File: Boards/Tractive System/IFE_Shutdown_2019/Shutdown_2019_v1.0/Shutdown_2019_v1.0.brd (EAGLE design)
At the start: 88.9 x 76.2 mm, 193 parts, among them Q1 DMN6140L-7, Q10 DMN6140L-7, Q11 DMP3099L-7, Q12 IRLML6346PBF, Q13 IRLML6346PBF, Q14 IRLML6346PBF, Q15 DMP3099L-7, Q16 DMN6140L-7, Q17 IRLML6346PBF, Q18 DMN6140L-7, Q2 DMN6140L-7, Q20 DMN6140L-7, Q21 DMN6140L-7, Q3 DMN6140L-7, Q4 DMN6140L-7, Q5 DMN6140L-7, Q6 DMP3099L-7, Q7 DMN6140L-7, Q9 DMN6140L-7, U1 STM32F103CBT6, U2 STM32F103CBT6

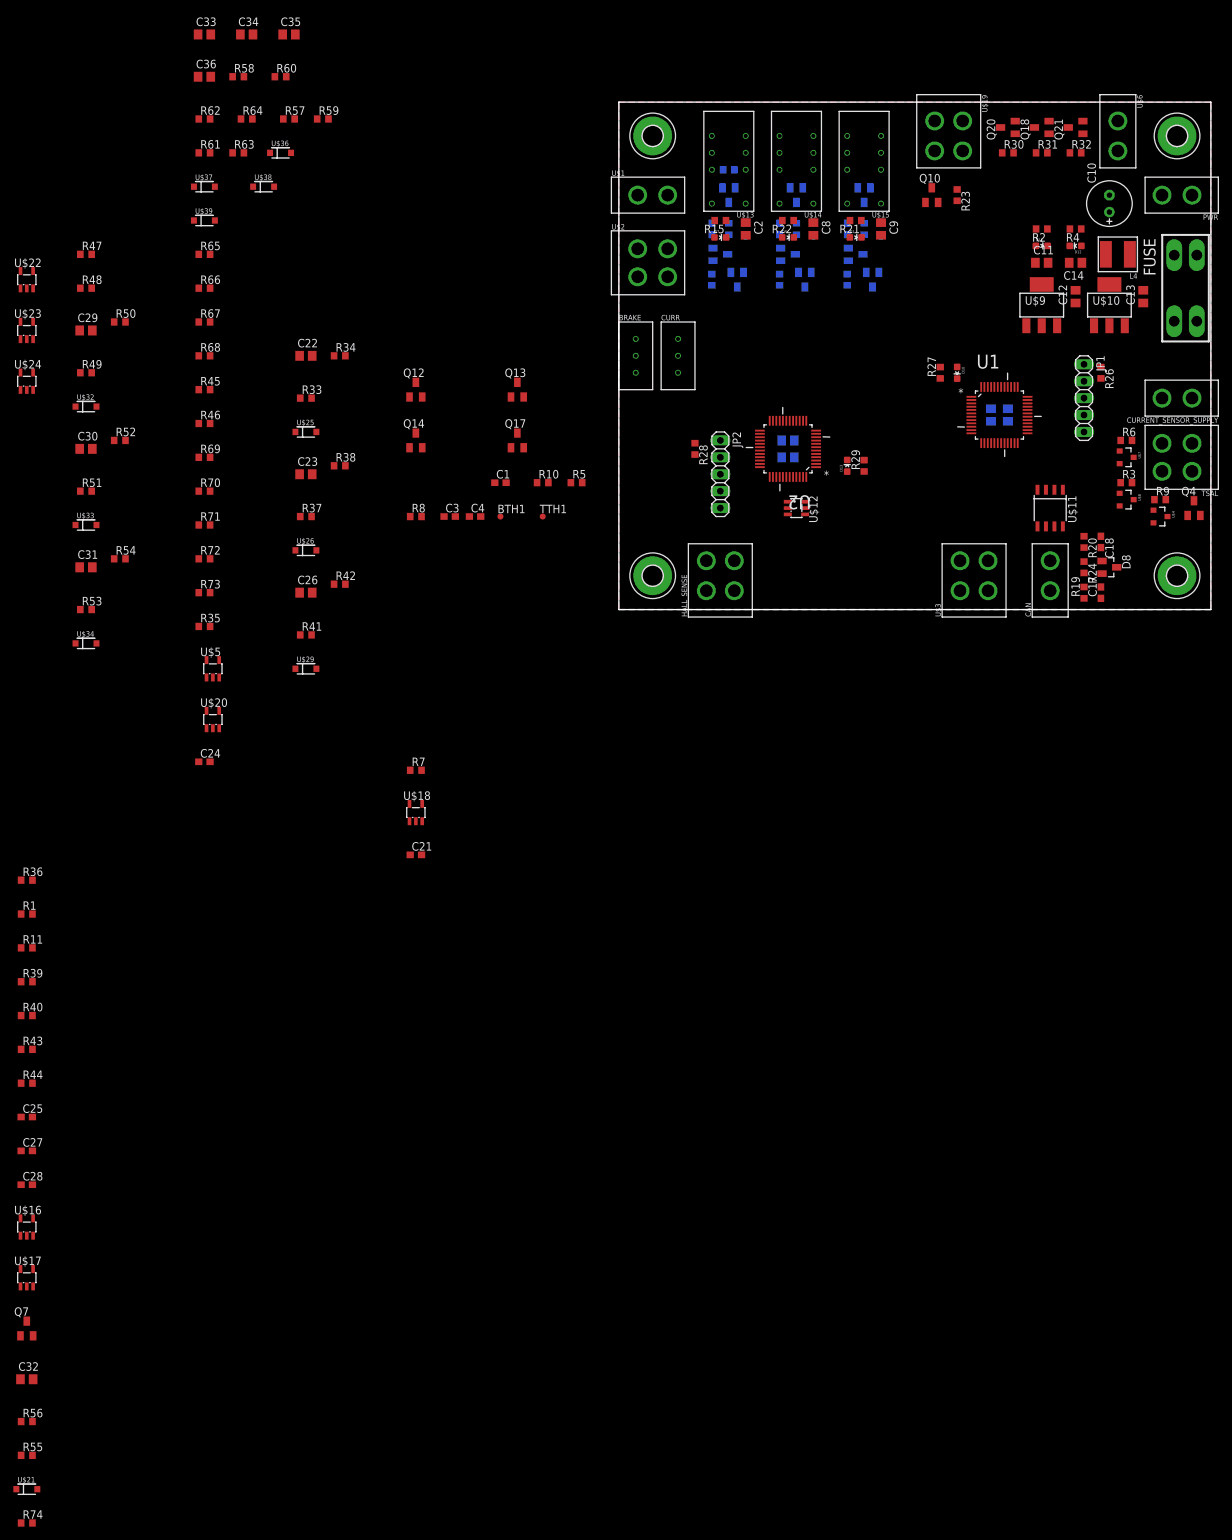
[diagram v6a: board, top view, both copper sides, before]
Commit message: Beginning initial Safety route
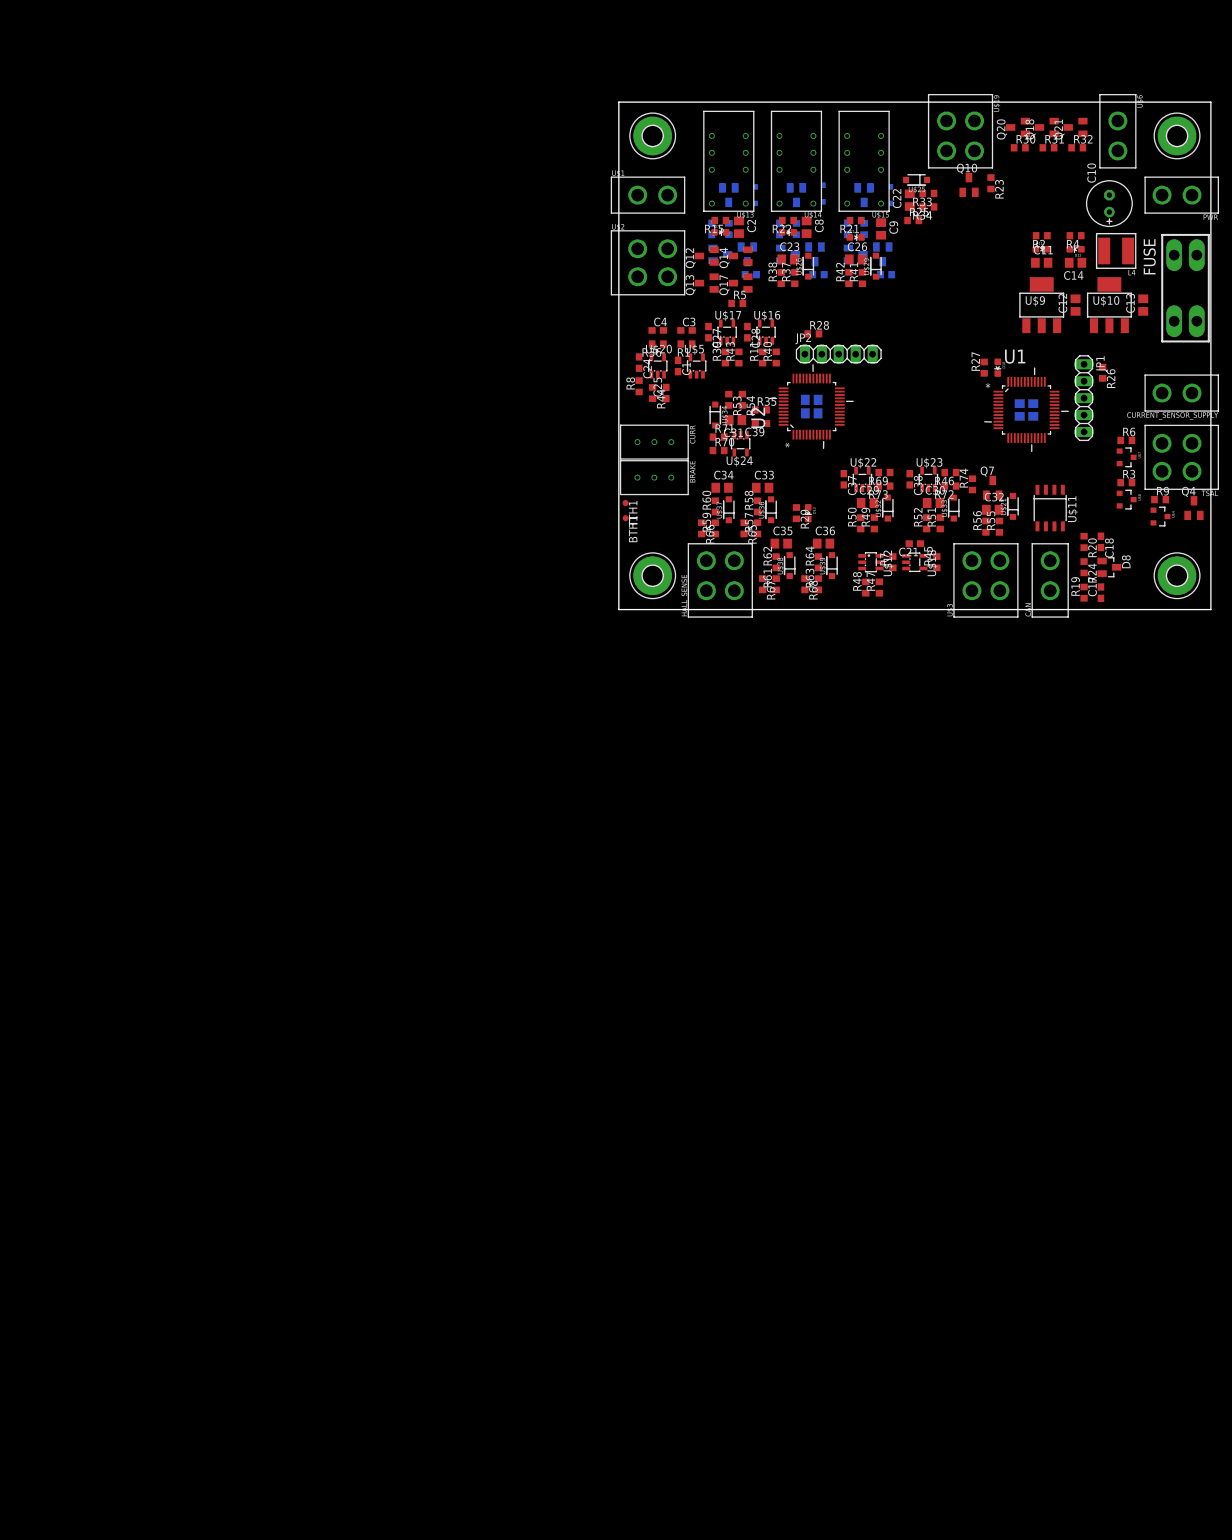
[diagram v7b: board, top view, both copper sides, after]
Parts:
- removed R10: 10k, resistor:R0603
- added C37, C38, C39: 0.1u, resistor:C0603
- R71, R72, R73: value 10k -> 15k
- moved R74 210.9 mm to (53.1, 18.8), turned to 90 degrees
- moved U$21 209.1 mm to (59.2, 15.5), turned to 90 degrees
- moved R55 201.9 mm to (57.1, 12.4), turned to 90 degrees
- moved R56 197.0 mm to (55.1, 12.4), turned to 90 degrees
- moved C32 195.1 mm to (56.1, 15.0)
- moved Q7 192.3 mm to (56.1, 18.3)
- moved U$17 176.7 mm to (16.3, 41.7)
- moved U$16 174.3 mm to (22.1, 41.7)
- moved C28 167.6 mm to (19.3, 41.7), turned to 270 degrees
- moved C27 160.0 mm to (13.5, 41.7), turned to 270 degrees
- moved R40 149.7 mm to (23.6, 37.8), turned to 90 degrees
- moved R43 149.1 mm to (18.0, 37.8), turned to 90 degrees
- moved C25 145.0 mm to (7.11, 32.5), turned to 90 degrees
- moved R11 141.7 mm to (21.6, 37.8), turned to 90 degrees
- moved R39 140.7 mm to (16.0, 37.8), turned to 90 degrees
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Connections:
- removed net FAULT_BSPD_F: C7.1, Q5.1, R16.2
- net +5V: now also C37.1, C38.1, C39.1; no longer R10.2
- net BRAKE_PRESSURE_F: no longer R10.1
- net FAULT_BSPD: now also C7.1, Q5.1, R16.2
- net GND: now also C37.2, C38.2, C39.2
- net THROTTLE_A: now also R49.1; no longer R51.1
- net THROTTLE_B: now also R51.1; no longer R49.1
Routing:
- removed copper zone on layer 1, net GND
- removed copper zone on layer 16, net GND

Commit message: nearly done with routing
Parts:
- removed R45: 10k, rcl:R0603
- moved C17 7.37 mm to (72.4, 9.91)
- moved R19 7.37 mm to (69.8, 9.91), turned to 270 degrees
- moved C18 7.37 mm to (72.4, 2.79), turned to 90 degrees
- moved R20 7.37 mm to (69.8, 2.79), turned to 90 degrees
- moved R11 6.35 mm to (15.2, 37.8)
- moved R39 5.08 mm to (21.1, 37.8)
- moved R43 0.76 mm to (17.3, 37.8)
- moved C15 0.51 mm to (59.7, 30.0)
- moved C19 0.51 mm to (62.7, 30.0)
- moved C16 0.51 mm to (29.0, 29.0)
- moved C20 0.51 mm to (29.0, 32.0)
- moved R40 0.51 mm to (23.1, 37.8)
- moved D9 0.25 mm to (30.7, 62.2)
- moved R23 0.25 mm to (55.6, 64.0)
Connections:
- net +5V: no longer R45.2
- net CANH: now also CAN.2; no longer CAN.1
- net CANL: now also CAN.1; no longer CAN.2
- net HALL_FL_F: now also U2.11; no longer U2.25
- net HALL_FR_F: now also U2.10; no longer U2.26
- net HALL_RL_F: now also U2.12; no longer U2.27
- net HALL_RR_F: now also U2.13; no longer U2.28
- net THROTTLE_OUT: no longer R45.1
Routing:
- net +5V: track 0.00 -> 241.0 mm, vias 0 -> 25
- net +3V3: track 0.00 -> 194.4 mm, vias 0 -> 13
- net +12V: track 0.00 -> 161.4 mm, vias 0 -> 4
- net FAULT_BSPD_STATUS_3_3: track 0.00 -> 70.7 mm, vias 0 -> 5
- net RTDS_EN: track 0.00 -> 62.8 mm, vias 0 -> 4
- net FAULT_BMS_STATUS_3_3: track 0.00 -> 57.2 mm, vias 0 -> 3
- net FAULT_IMD_STATUS_3_3: track 0.00 -> 48.9 mm, vias 0 -> 3
- net RTD_EN: track 0.00 -> 47.2 mm, vias 0 -> 2
- net BRAKE_PRESSURE_F_3_3: track 0.00 -> 46.3 mm, vias 0 -> 4
- net HV_CONNECTED_3_3: track 0.00 -> 45.8 mm
- net AIR_OUT: track 0.00 -> 45.8 mm
- net BTSF_EN: track 0.00 -> 44.4 mm, vias 0 -> 2
- net APPS_EN: track 0.00 -> 43.9 mm
- net FAULT_RESET_F: track 0.00 -> 43.5 mm, vias 0 -> 3
- net FAULT_IMD: track 0.00 -> 39.0 mm, vias 0 -> 1
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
